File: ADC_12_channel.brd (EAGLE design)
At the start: 148.1 x 127 mm, 166 parts, among them IC1 LM317BD2T, IC2 LM317BD2T, K1 691131710003, K2 691101710002, K3 691101710002, K4 691101710002, K5 691101710002, K6 691101710002, K7 691101710002, K8 691101710002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

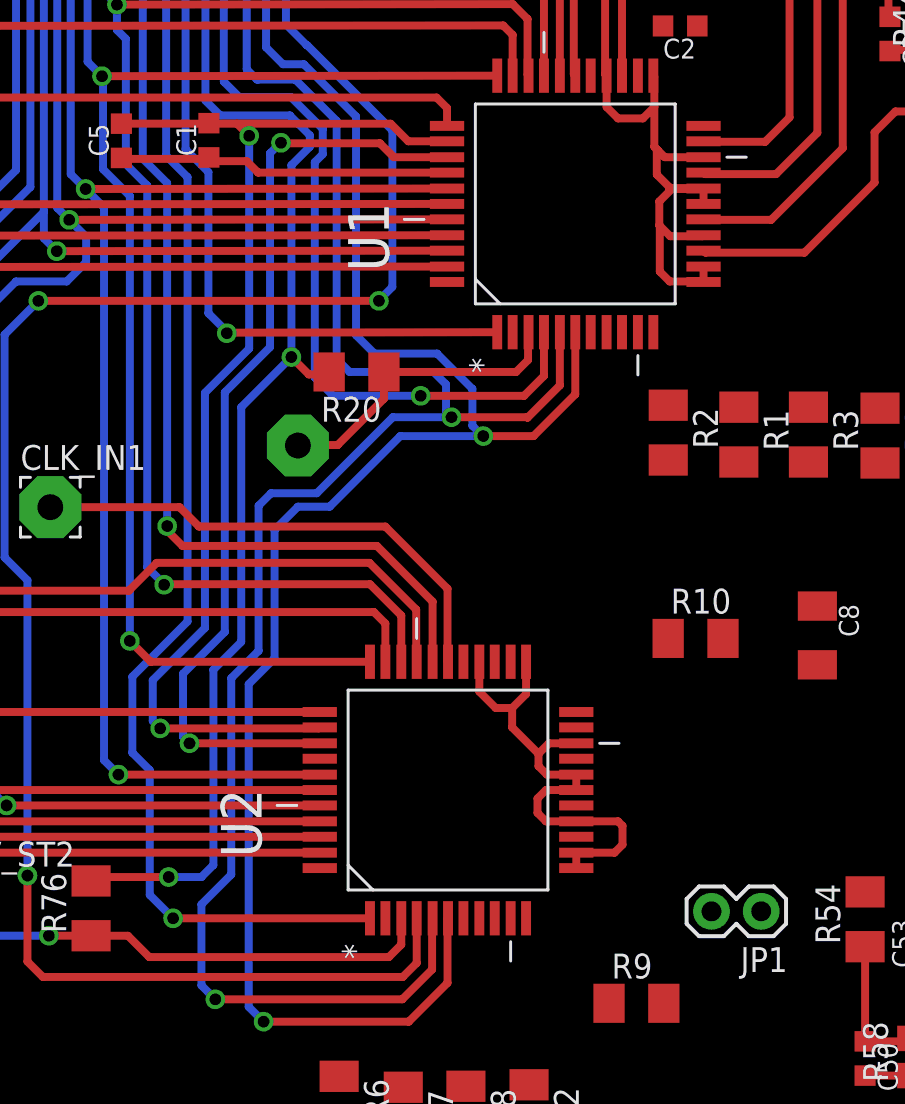
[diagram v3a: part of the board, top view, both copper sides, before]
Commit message: joined AVdd and DVdd
It was of no use, due to lack of two seperate regulator IC.
reduced component and simplified the circuit.
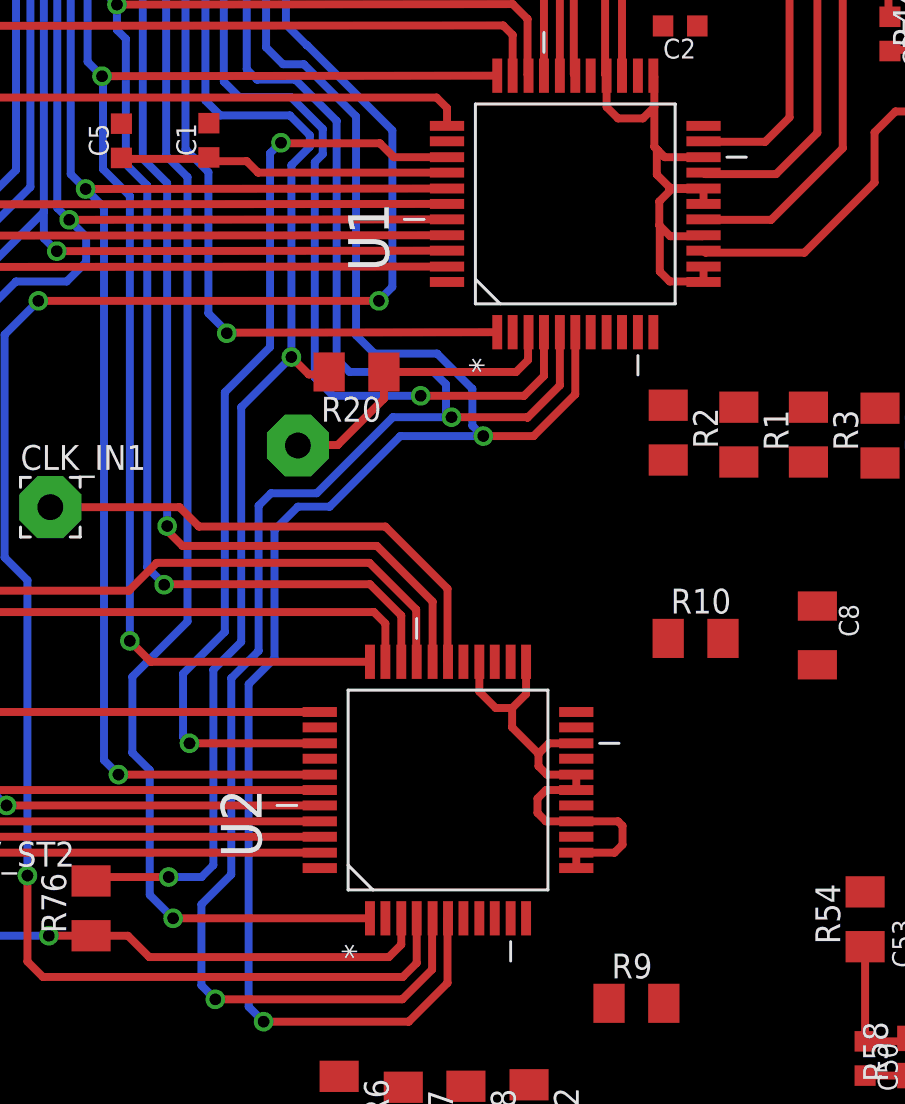
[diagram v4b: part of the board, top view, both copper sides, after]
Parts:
- removed JP1: (no value), SparkFun-Retired:1X02
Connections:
- removed net DVDD: C1.2, C5.2, JP1.2, U1.35, U2.35
- net VDD: now also C1.2, C5.2, U1.35, U2.35; no longer JP1.1
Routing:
- net DVDD: track 58.8 -> 0.00 mm, vias 2 -> 0
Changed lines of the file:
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@@
 </element>
 <element name="C8" library="rcl" package="C1206K" value="47u" x="56.0578" y="-3.6576" rot="R270"/>
-<element name="JP1" library="SparkFun-Retired" package="1X02" value="" x="53.1876" y="-17.7546" rot="R180"/>
 <element name="R1" library="resistor" package="M1206" value="10k" x="52.0446" y="6.604" rot="R270"/>
 <element name="R10" library="resistor" package="M1206" value="10k" x="49.8348" y="-3.81"/>
@@
 <wire x1="22.8346" y1="1.7018" x2="23.622" y2="0.9144" width="0.4064" layer="1"/>
 </signal>
-<signal name="DVDD">
-<contactref element="U1" pad="35"/>
-<contactref element="C1" pad="2"/>
-<contactref element="JP1" pad="2"/>
-<contactref element="U2" pad="35"/>
-<contactref element="C5" pad="2"/>
-<wire x1="37.1348" y1="21.59" x2="35.1536" y2="21.59" width="0.4064" layer="1"/>
-<wire x1="25.0546" y1="22.5044" x2="24.9682" y2="22.5158" width="0.4064" layer="1"/>
-<wire x1="20.4978" y1="22.4904" x2="24.8666" y2="22.4892" width="0.4064" layer="1"/>
-<wire x1="24.8666" y1="22.4892" x2="24.9682" y2="22.5158" width="0.4064" layer="1"/>
-<wire x1="24.9834" y1="22.606" x2="24.9682" y2="22.5158" width="0.4064" layer="1"/>
-<wire x1="26.4058" y1="22.4892" x2="34.2544" y2="22.4892" width="0.4064" layer="1"/>
-<wire x1="34.2544" y1="22.4892" x2="35.1536" y2="21.59" width="0.4064" layer="1"/>
-<wire x1="24.8666" y1="22.4892" x2="26.4058" y2="22.4892" width="0.4064" layer="1"/>
-<wire x1="26.4058" y1="22.4892" x2="27.0256" y2="21.8694" width="0.4064" layer="1"/>
-<via x="27.0256" y="21.8694" extent="1-16" drill="0.6"/>
-<wire x1="27.0256" y1="21.8694" x2="27.0256" y2="10.9982" width="0.4064" layer="16"/>
-<wire x1="27.0256" y1="10.9982" x2="24.765" y2="8.7376" width="0.4064" layer="16"/>
-<wire x1="24.765" y1="8.7376" x2="24.765" y2="-3.2766" width="0.4064" layer="16"/>
-<wire x1="24.765" y1="-3.2766" x2="22.098" y2="-5.9436" width="0.4064" layer="16"/>
-<wire x1="22.098" y1="-5.9436" x2="22.098" y2="-8.0264" width="0.4064" layer="16"/>
-<wire x1="22.098" y1="-8.0264" x2="22.479" y2="-8.4074" width="0.4064" layer="16"/>
-<via x="22.479" y="-8.4074" extent="1-16" drill="0.6"/>
-<wire x1="22.479" y1="-8.4074" x2="30.5816" y2="-8.4074" width="0.4064" layer="1"/>
-<wire x1="30.5816" y1="-8.4074" x2="30.6324" y2="-8.3566" width="0.4064" layer="1"/>
-<wire x1="34.2544" y1="22.4892" x2="50.6476" y2="-17.7546" width="0" layer="19" extent="1-1"/>
-</signal>
 <signal name="N$13">
 <contactref element="U1" pad="10"/>
@@
 <contactref element="C3" pad="2"/>
 <contactref element="C4" pad="2"/>
-<contactref element="JP1" pad="1"/>
 <contactref element="R5" pad="2"/>
 <contactref element="R9" pad="2"/>
@@
 <wire x1="119.9388" y1="29.083" x2="119.9388" y2="32.8168" width="0.8128" layer="1"/>
 <wire x1="119.9388" y1="32.8168" x2="119.9896" y2="32.8676" width="0.8128" layer="1"/>
+<contactref element="C1" pad="2"/>
+<contactref element="U1" pad="35"/>
+<contactref element="C5" pad="2"/>
+<contactref element="U2" pad="35"/>
 <wire x1="61.6428" y1="19.812" x2="119.9388" y2="29.083" width="0" layer="19" extent="1-1"/>
 <wire x1="59.2582" y1="5.1532" x2="61.6428" y2="19.812" width="0" layer="19" extent="1-1"/>
@@
 <wire x1="64.4398" y1="-5.691" x2="56.0578" y2="-5.1576" width="0" layer="19" extent="1-1"/>
 <wire x1="39.5732" y1="-5.0038" x2="51.2348" y2="-3.81" width="0" layer="19" extent="1-1"/>
-<wire x1="53.1876" y1="-17.7546" x2="56.0578" y2="-5.1576" width="0" layer="19" extent="1-1"/>
-<wire x1="48.2122" y1="-22.4536" x2="53.1876" y2="-17.7546" width="0" layer="19" extent="1-1"/>
+<wire x1="30.6324" y1="-8.3566" x2="39.5732" y2="-5.0038" width="0" layer="19" extent="1-1"/>
+<wire x1="46.0756" y1="24.9428" x2="61.6428" y2="19.812" width="0" layer="19" extent="1-1"/>
+<wire x1="37.1348" y1="21.59" x2="46.0756" y2="24.9428" width="0" layer="19" extent="1-1"/>
+<wire x1="24.9682" y1="22.5158" x2="37.1348" y2="21.59" width="0" layer="19" extent="1-1"/>
+<wire x1="20.4978" y1="22.4904" x2="24.9682" y2="22.5158" width="0" layer="19" extent="1-1"/>
+<wire x1="48.2122" y1="-22.4536" x2="51.2348" y2="-3.81" width="0" layer="19" extent="1-1"/>
 <wire x1="38.1" y1="-29.4924" x2="48.2122" y2="-22.4536" width="0" layer="19" extent="1-1"/>
 <wire x1="34.8996" y1="-29.5432" x2="38.1" y2="-29.4924" width="0" layer="19" extent="1-1"/>
 <wire x1="31.623" y1="-28.9844" x2="34.8996" y2="-29.5432" width="0" layer="19" extent="1-1"/>
-<wire x1="46.0756" y1="24.9428" x2="61.6428" y2="19.812" width="0" layer="19" extent="1-1"/>
 </signal>
 <signal name="N$16">

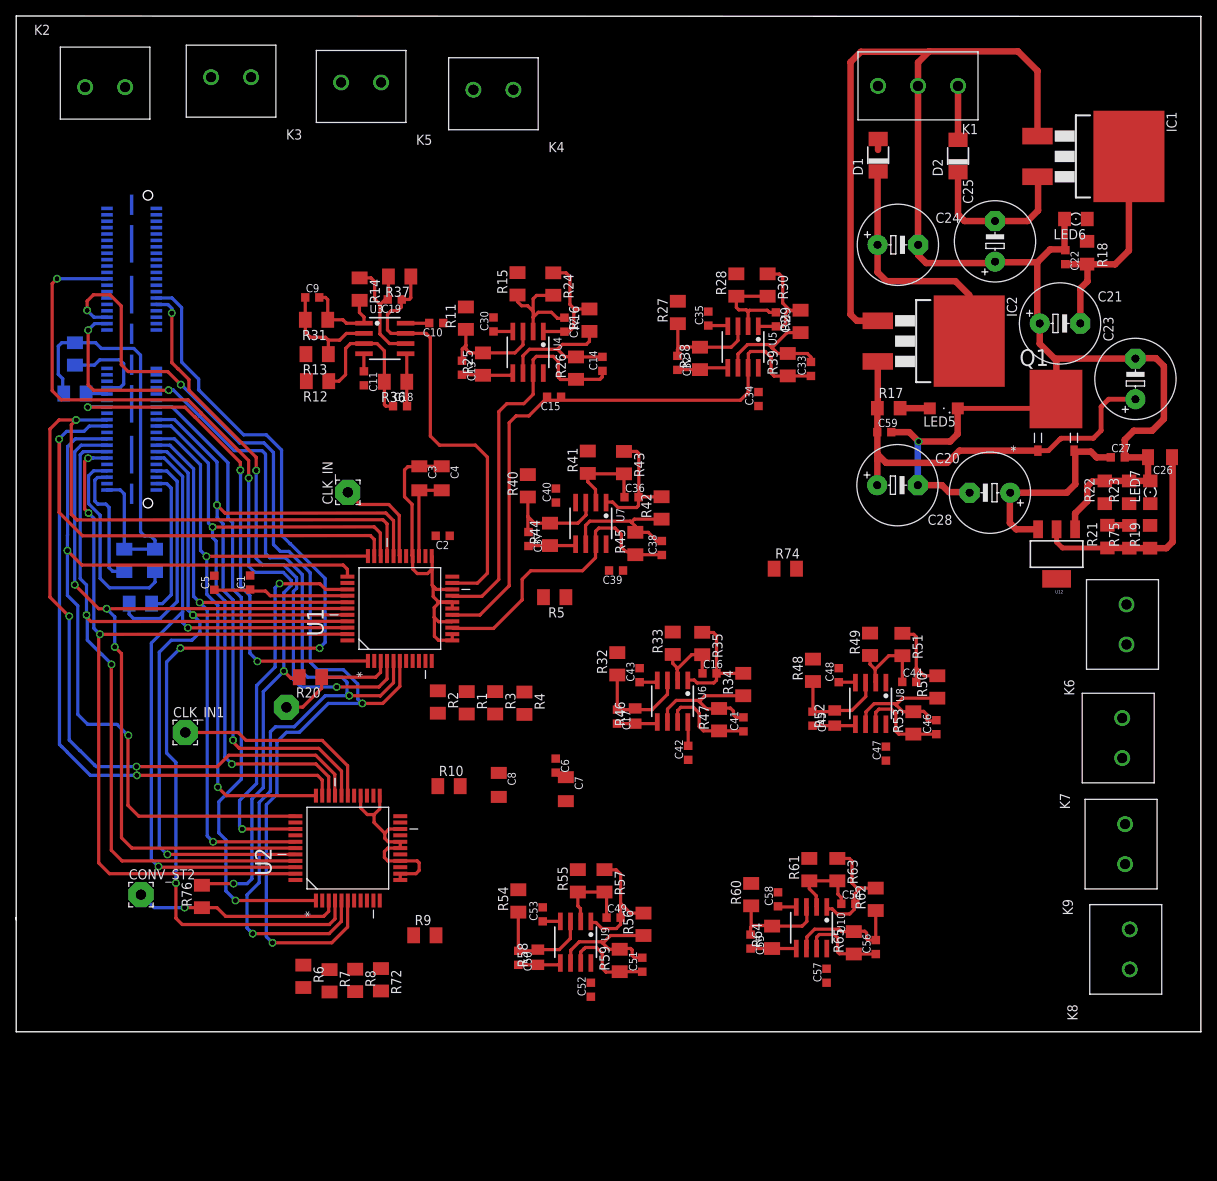
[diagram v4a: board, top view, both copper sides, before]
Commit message: Re-arranged ADC1 opamps
Filled up the gap around the header,
jigsawed them for proper space usage.

Next commit ADC1 peripheral components
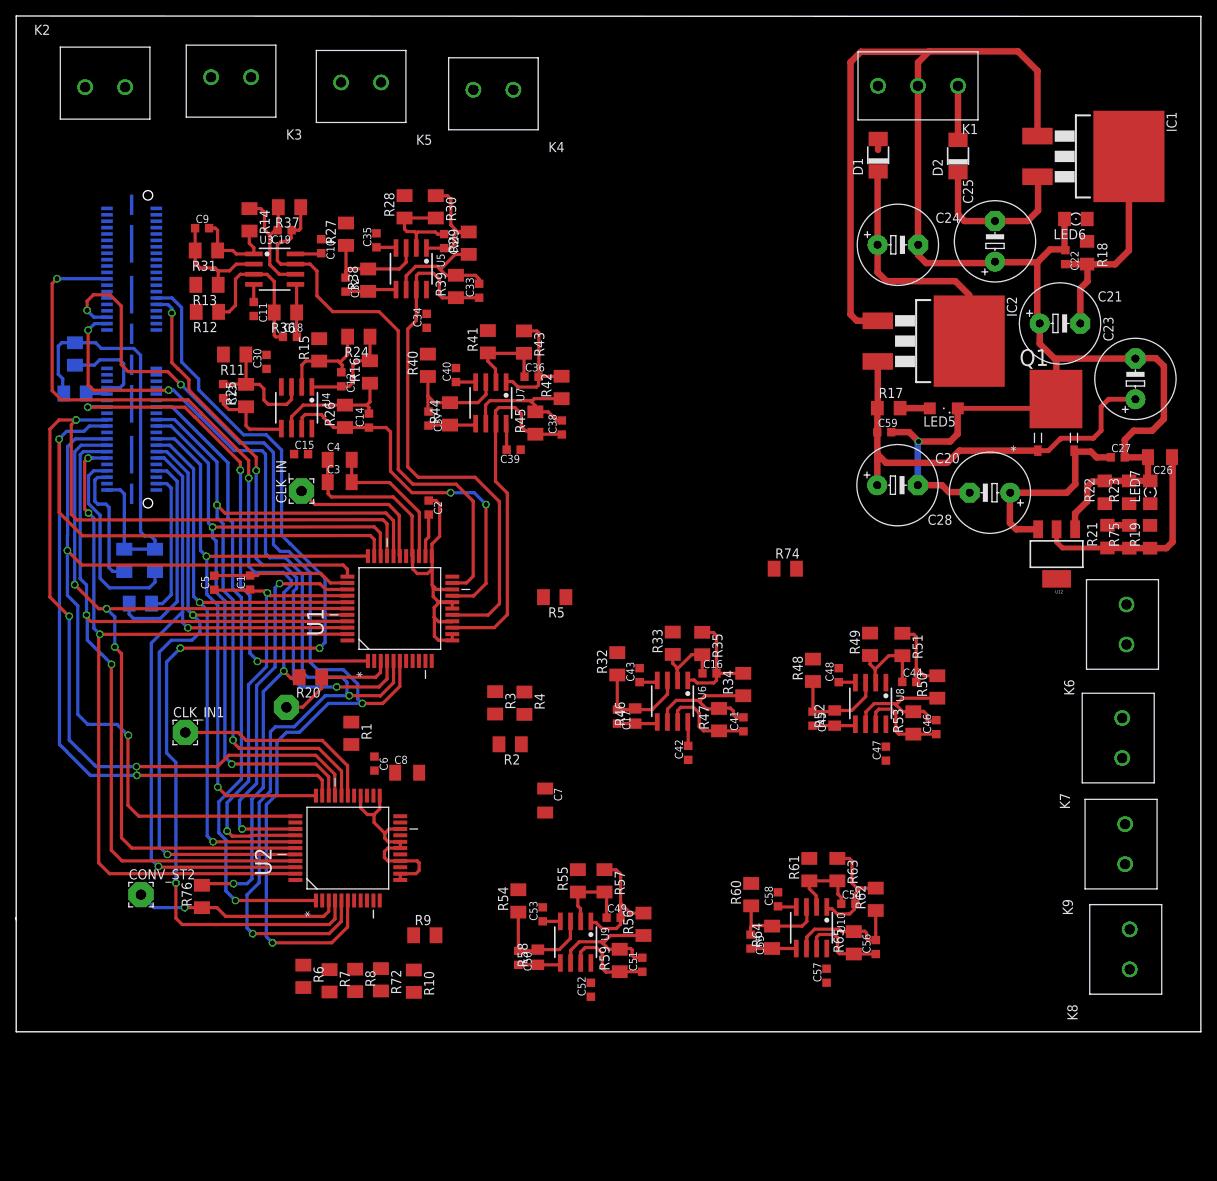
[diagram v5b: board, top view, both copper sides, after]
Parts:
- moved C34 42.6 mm to (47.0, 54.4)
- moved R30 42.6 mm to (48.2, 68.6)
- moved C31 42.6 mm to (49.2, 64.3)
- moved C32 42.6 mm to (36.9, 58.9)
- moved R28 42.6 mm to (44.3, 68.6)
- moved R38 42.6 mm to (39.7, 59.4)
- moved U5 42.6 mm to (45.1, 60.9)
- moved C33 42.6 mm to (53.6, 58.1)
- moved C35 42.6 mm to (40.8, 64.4)
- moved R27 42.6 mm to (37.0, 65.2)
- moved R29 42.6 mm to (52.3, 64.1)
- moved R39 42.6 mm to (50.7, 58.6)
- moved C15 32.4 mm to (31.3, 37.7), turned to 0 degrees
- moved C14 30.0 mm to (39.8, 41.9)
- moved C13 30.0 mm to (21.6, 45.6)
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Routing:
- net DGND: track 240.7 -> 281.4 mm, vias 1 -> 3
- net VDD: track 36.5 -> 61.0 mm
- net AGND: track 117.5 -> 135.9 mm
- net ADC1: track 54.6 -> 70.2 mm
- net ADC3: track 75.7 -> 67.3 mm
- net ADC4: track 37.2 -> 44.4 mm
- net N$11: track 12.8 -> 18.6 mm
- net N$16: track 0.00 -> 5.36 mm
- net VCC_12+: track 59.2 -> 62.8 mm
- net N$46: track 18.5 -> 15.6 mm
- net ADC2: track 49.3 -> 46.9 mm, vias 0 -> 2
- net N$33: track 15.1 -> 12.8 mm
- net N$34: track 14.9 -> 12.9 mm
- net N$45: track 14.0 -> 16.0 mm

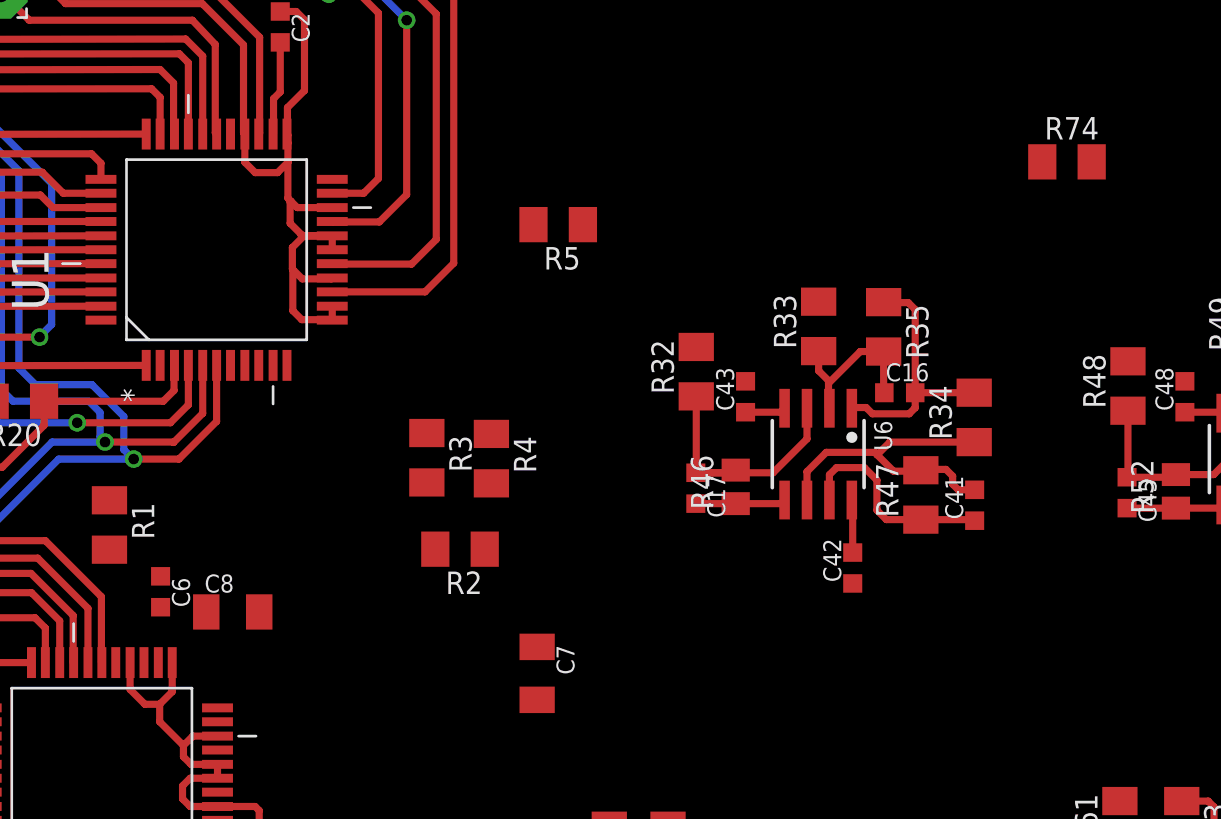
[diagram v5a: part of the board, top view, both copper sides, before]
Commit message: Finished all peripherals of ADC1
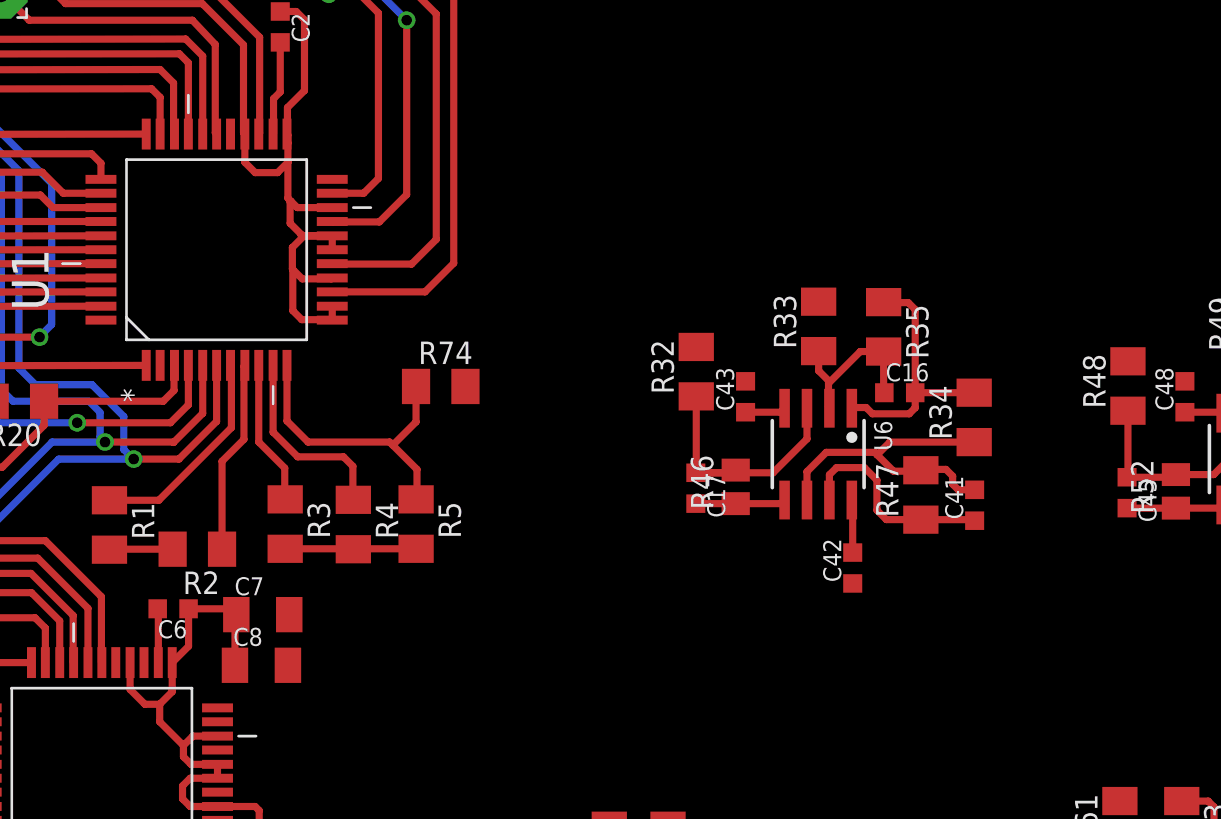
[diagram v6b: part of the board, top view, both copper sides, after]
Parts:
- moved R74 37.7 mm to (56.4, 10.6)
- moved R5 18.8 mm to (55.0, 2.84), turned to 270 degrees
- moved C7 15.9 mm to (46.3, -2.29), turned to 0 degrees
- moved R2 14.9 mm to (42.6, 1.42)
- moved R3 8.86 mm to (47.6, 2.84)
- moved R4 8.67 mm to (51.4, 2.82)
- moved C8 3.43 mm to (46.2, -5.16)
- moved C6 1.20 mm to (41.2, -1.96), turned to 180 degrees
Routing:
- net N$19: track 0.00 -> 17.2 mm
- net N$17: track 0.00 -> 12.2 mm
- net VDD: track 61.0 -> 72.0 mm
- net N$13: track 0.00 -> 11.0 mm
- net N$15: track 0.00 -> 10.9 mm
- net AGND: track 135.9 -> 145.1 mm
- net N$14: track 0.00 -> 8.21 mm
- net N$24: track 0.00 -> 3.06 mm
